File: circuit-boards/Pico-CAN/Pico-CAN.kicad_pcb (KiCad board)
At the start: 2 copper layers, 70 x 53 mm, 19 parts, among them J1 CAN1, J2 CAN1, J3 Expansion, U1 4.0 MHz, U2 MCP2558FD, U3 MCP2518FDT-H/SL

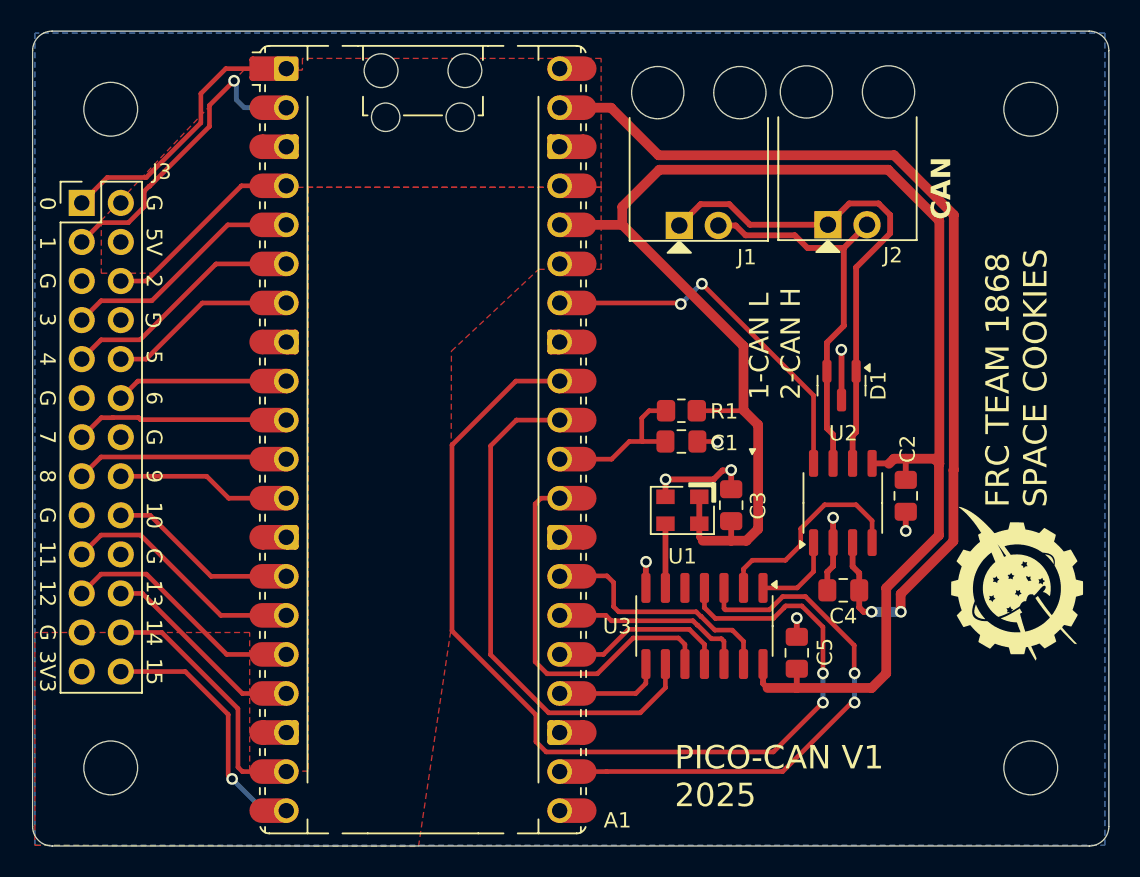
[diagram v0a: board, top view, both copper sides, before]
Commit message: Minor update to PicoCAN. Add JLC assembly docs
Signed-off-by: Scott Berman <sgberman1@gmail.com>
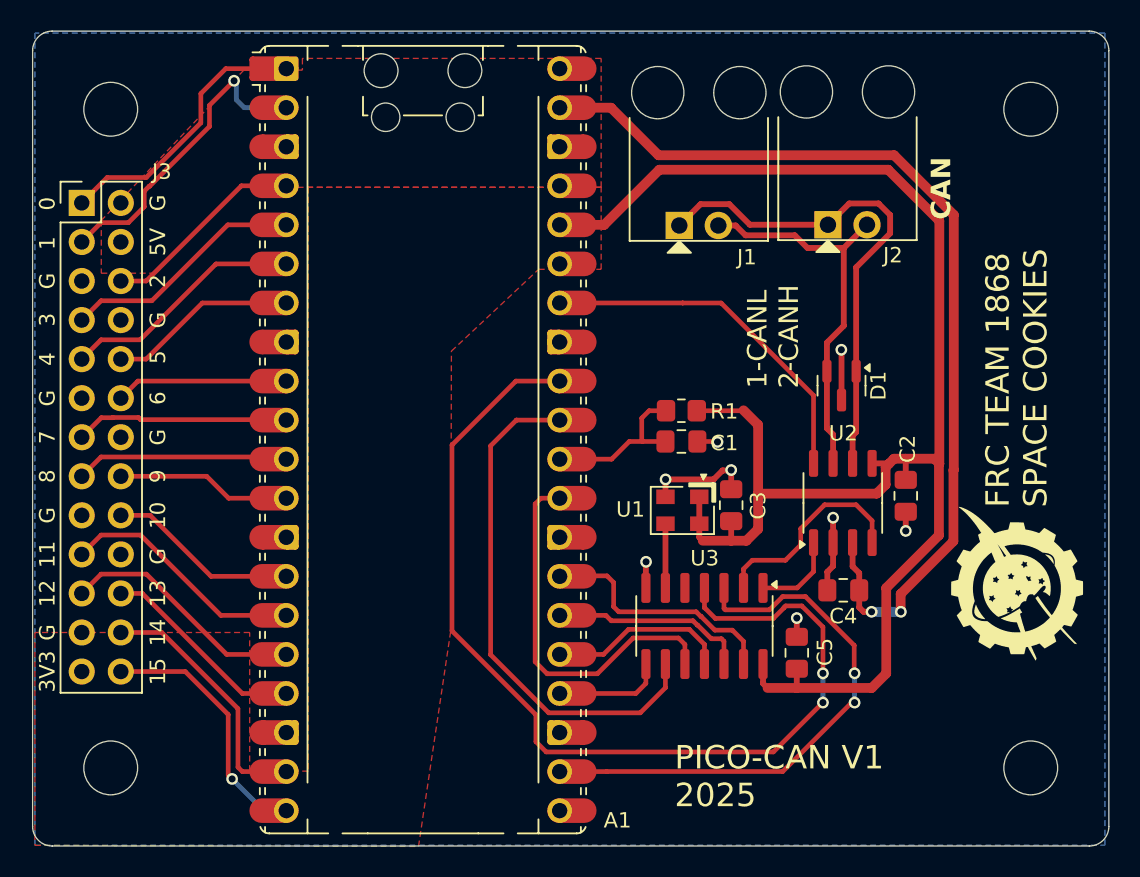
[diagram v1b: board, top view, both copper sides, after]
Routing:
- net +3V3: track 110.0 -> 104.0 mm
- net /XCVR_STBY: track 23.7 -> 22.6 mm, vias 2 -> 0
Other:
- board text added: "1-CANL 2-CANH"
- board text removed: "1-CAN L 2-CAN H"

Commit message: Checkin post review
Signed-off-by: Scott Berman <sgberman1@gmail.com>
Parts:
- moved C2 3.94 mm to (210.3, 131.4), turned to 180 degrees
- moved R1 0.33 mm to (210.3, 127.4)
- moved C1 0.30 mm to (210.3, 129.4)
- renumbered C3 to C2, C2 to C3, J3 to J1, J1 to J2, J2 to J3, U2 to U1, U1 to U2
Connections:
- A1 pad 21: unconnected-(A1-GPIO16-Pad21)_1 -> /START_OF_FRAME
- A1 pad 22: /START_OF_FRAME -> /~{CAN_IRQ}
- A1 pad 32: /~{CAN_IRQ} -> unconnected-(A1-GPIO27_ADC1-Pad32)
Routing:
- net /~{CAN_IRQ}: track 65.8 -> 33.5 mm
- net +3V3: track 104.0 -> 100.3 mm
- net GND: track 20.2 -> 16.6 mm, vias 8 -> 7
- net /START_OF_FRAME: track 35.7 -> 38.2 mm
- net /XCVR_STBY: track 22.6 -> 21.3 mm
- net /GPIO15: track 16.8 -> 16.0 mm
- net /GPIO14: track 16.7 -> 16.0 mm
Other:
- outline, holes or cut-outs redrawn
- board text added: "ADC1"
- board text added: "ADCREF"
- board text added: "CS"
- board text added: "EN"
- board text added: "GND"
- board text added: "GP0"
- board text added: "GP1"
- board text added: "GP10"
- board text added: "GP11"
- board text added: "GP12"
- board text added: "GP13"
- board text added: "GP14"
- board text added: "GP15"
- board text added: "GP2"
- board text added: "GP3"
- board text added: "GP4"
- board text added: "GP5"
- board text added: "GP6"
- board text added: "GP7"
- board text added: "GP8"
- board text added: "GP9"
- board text added: "IRQ"
- board text added: "MI"
- board text added: "MO"
- board text added: "RUN"
- board text added: "RXI"
- board text added: "SCK"
- board text added: "SILENT"
- board text added: "SOF"
- board text added: "TXI"
- board text added: "VBUS"

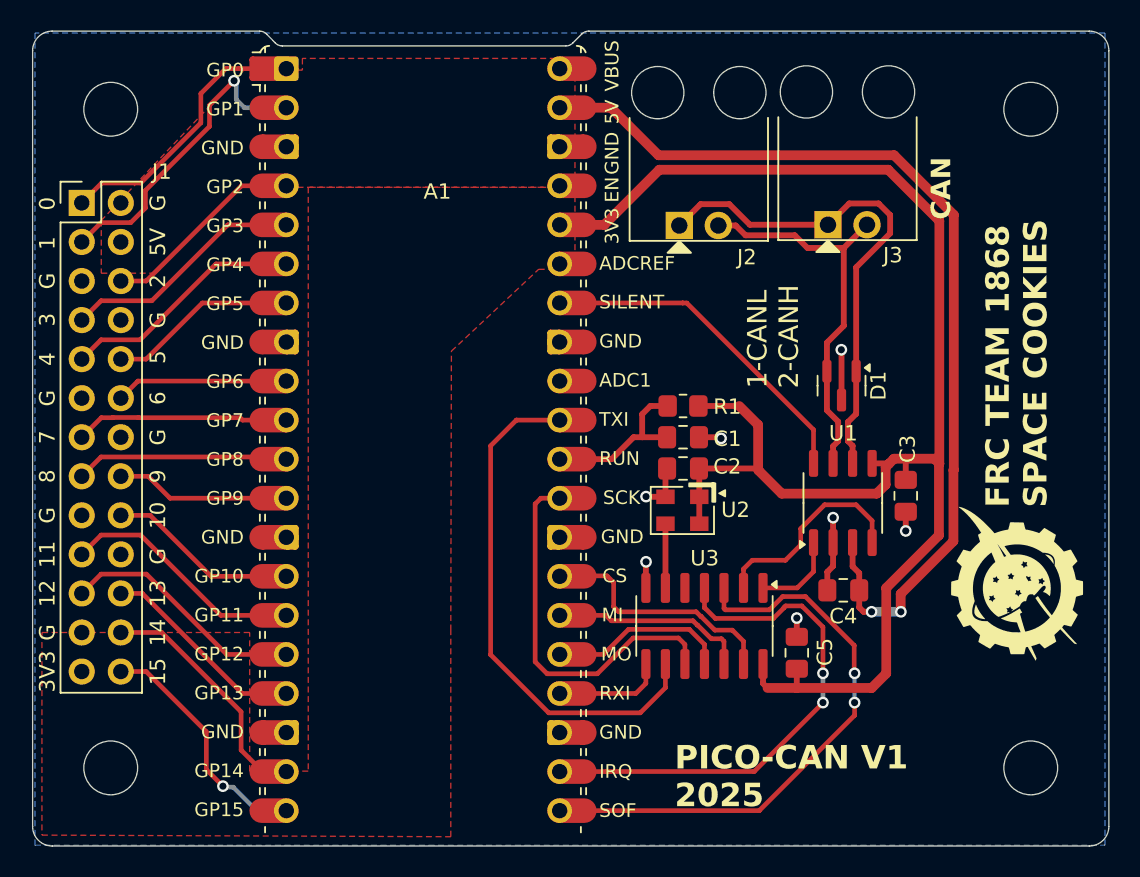
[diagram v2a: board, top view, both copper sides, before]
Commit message: Changed oscillator back to ECS5032
Signed-off-by: Scott Berman <sgberman1@gmail.com>
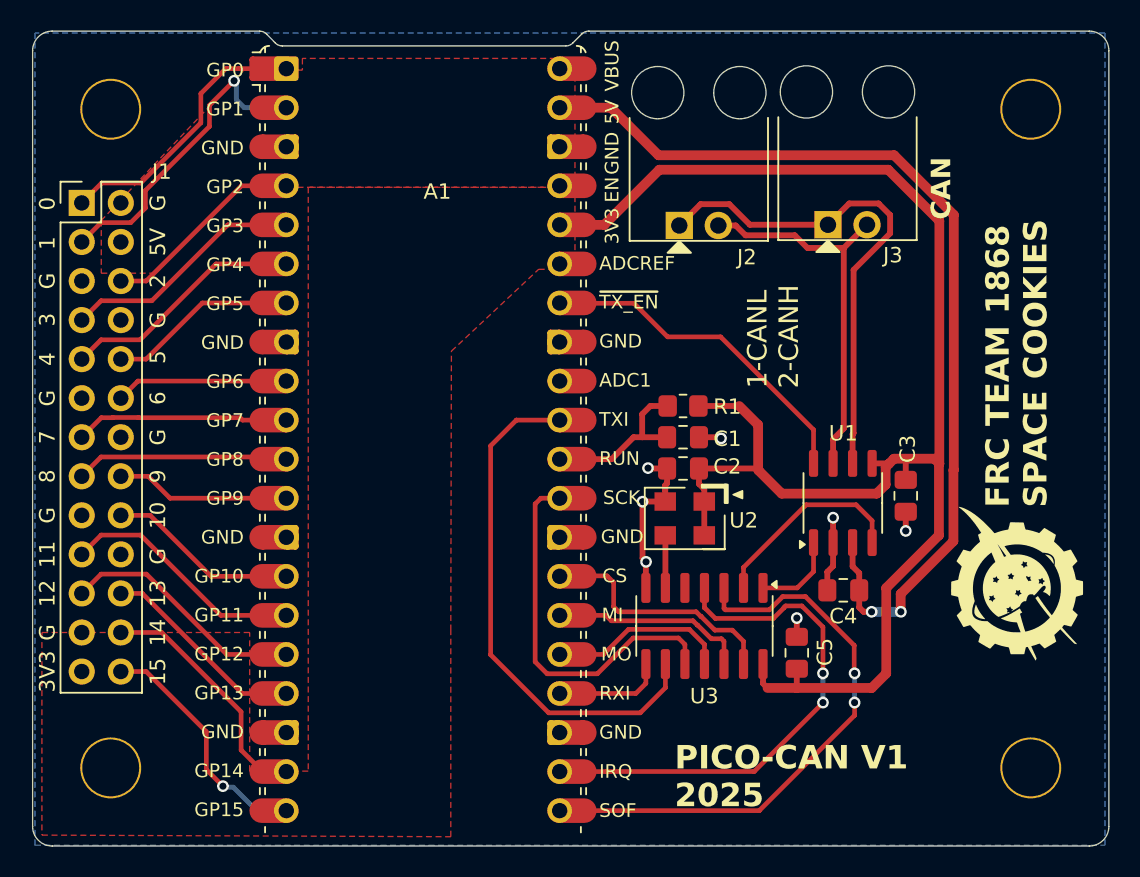
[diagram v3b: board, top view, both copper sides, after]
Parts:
- removed D1: PESD1CAN, Package_TO_SOT_SMD:SOT-23
- H1, H2, H3, H4: footprint MountingHole:MountingHole_3.5mm -> MountingHole:MountingHole_3.7mm
- U2: footprint Pico-CAN:JLC-OSC-SMD3225-4P -> Pico-CAN:ECS-5032MV
- moved U2 0.55 mm to (210.4, 134.7)
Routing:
- net GND: track 16.6 -> 19.2 mm
- net Net-(U2-OUT): track 4.18 -> 3.43 mm
- net +3V3: track 100.3 -> 101.0 mm
- net /CAN_H: track 25.8 -> 25.2 mm
- net /CANRX: track 13.8 -> 13.2 mm
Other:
- board text added: "~{TX_EN}"
- board text removed: "SILENT"

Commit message: Update BOM
Signed-off-by: Scott Berman <sgberman1@gmail.com>
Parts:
- J2, J3: value CAN1 -> CAN
